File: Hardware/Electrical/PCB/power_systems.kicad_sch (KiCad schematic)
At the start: 11 parts, among them U2 LMR50410

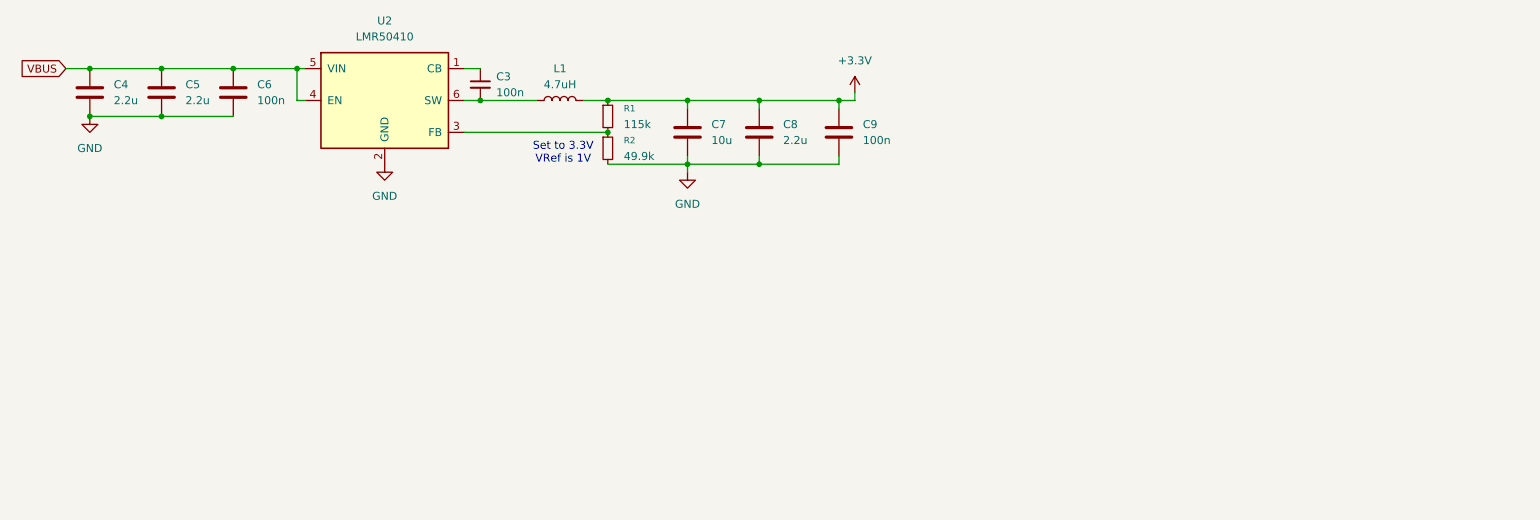
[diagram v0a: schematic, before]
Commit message: battery charger added
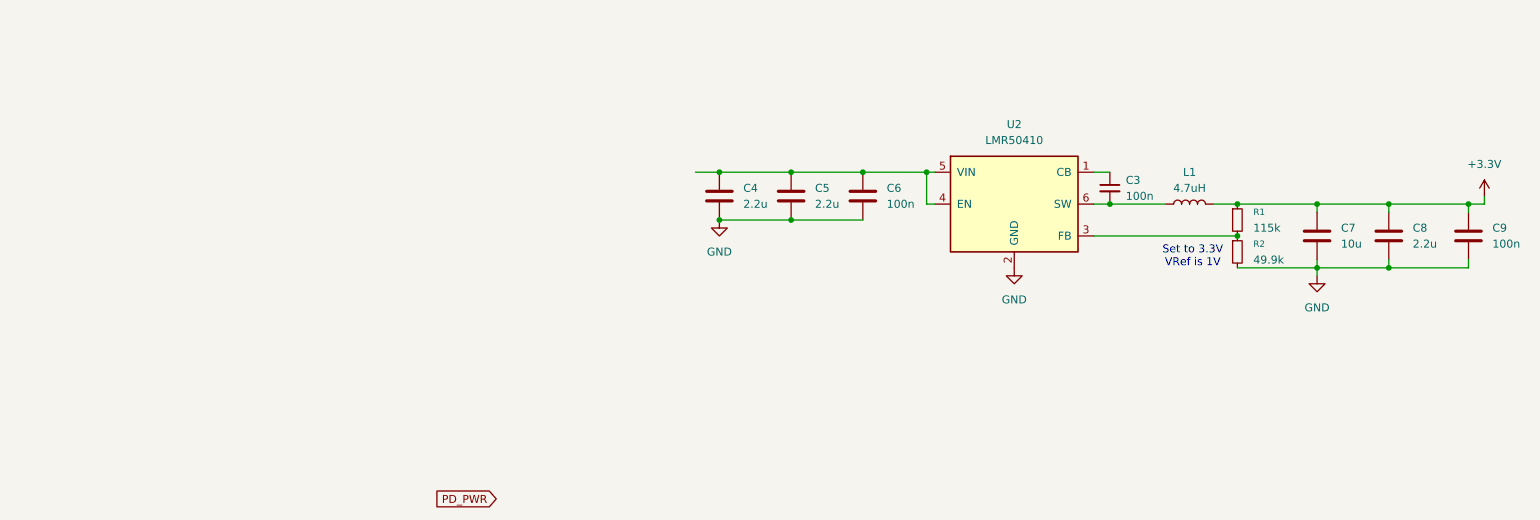
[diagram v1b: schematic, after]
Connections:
- net VBUS: no longer names the net of C4.1, C5.1, C6.1, U2.4 (EN), U2.5 (VIN)
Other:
- moved on the sheet: C3, C4, C5, C6, C7, C8, C9, L1, R1, R2, U2

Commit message: project state at start of school project
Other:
- moved on the sheet: C3, C4, C5, C6, C7, C8, C9, L1, R1, R2, U2

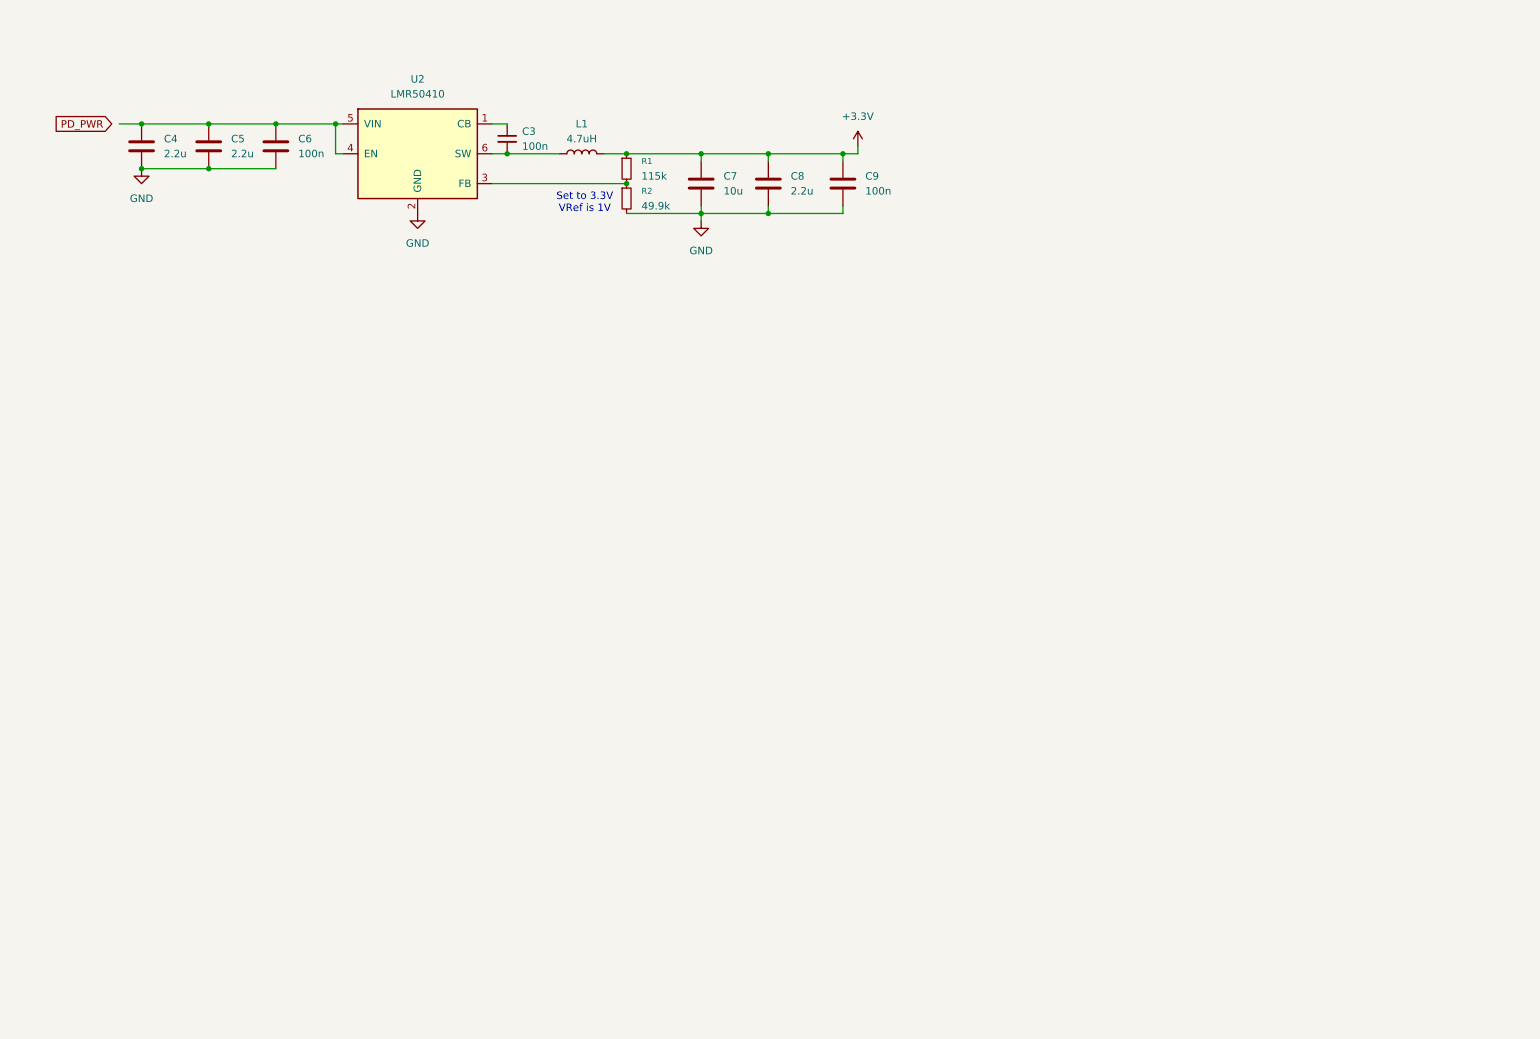
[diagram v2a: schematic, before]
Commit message: Basic Schematic finished, external connectors missing, no footprints or LCSC numbers yet
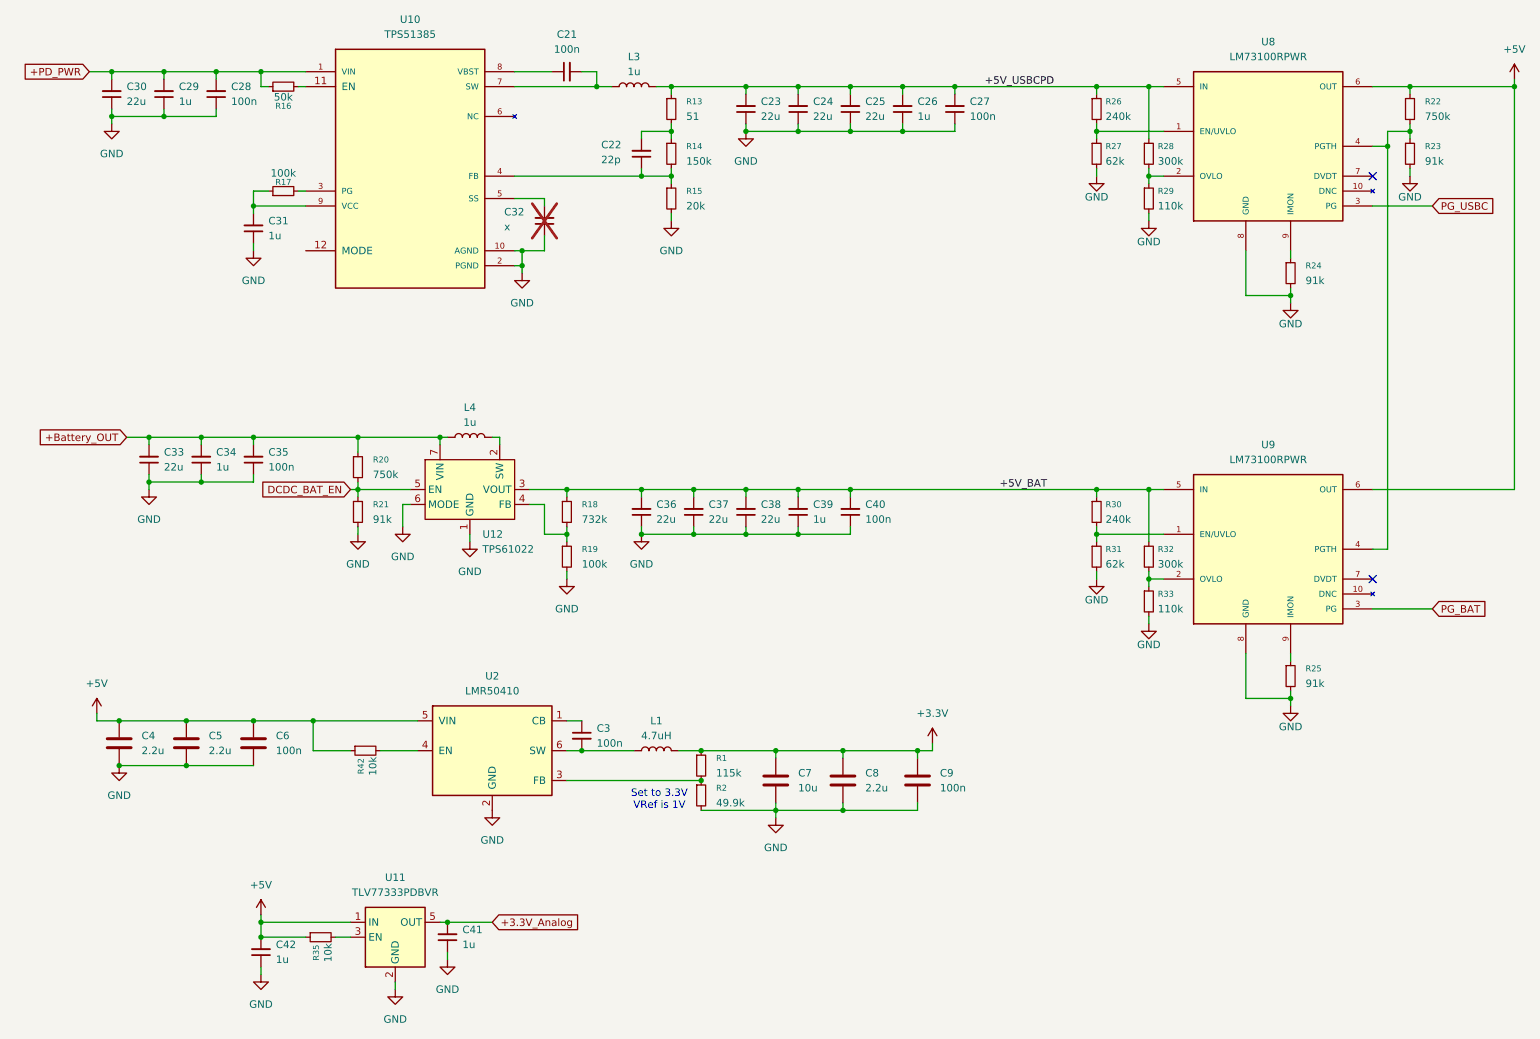
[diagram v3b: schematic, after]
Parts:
- added C21, C27, C28, C35, C40: 100n, symbol Device:C_Small
- added C22: 22p, symbol Device:C_Small
- added C23, C24, C25, C30, C33, C36, C37, C38: 22u, symbol Device:C_Small
- added C26, C29, C31, C34, C39, C41, C42: 1u, symbol Device:C_Small
- added C32: x, symbol Device:C_Small
- added L3, L4: 1u, symbol Device:L
- added R13: 51, symbol Device:R_Small
- added R14: 150k, symbol Device:R_Small
- added R15: 20k, symbol Device:R_Small
- added R16: 50k, symbol Device:R_Small
- added R17, R19: 100k, symbol Device:R_Small
- added R18: 732k, symbol Device:R_Small
- added R20, R22: 750k, symbol Device:R_Small
- added R21, R23, R24, R25: 91k, symbol Device:R_Small
- added R26, R30: 240k, symbol Device:R_Small
- added R27, R31: 62k, symbol Device:R_Small
- added R28, R32: 300k, symbol Device:R_Small
- added R29, R33: 110k, symbol Device:R_Small
- added R35, R42: 10k, symbol Device:R_Small
- added U10: TPS51385, symbol TPS51385:LM73100RPWR
- added U11: TLV77333PDBVR, Package_TO_SOT_SMD:SOT-23-5, symbol Regulator_Linear:TPS77033PDBV
- added U12: TPS61022, Package_DFN_QFN:Texas_RWU0007A_VQFN-7_2x2mm_P0.5mm, symbol Converter_DCDC:TPS61022
- added U8, U9: LM73100RPWR, LM73100RPWR:IC_LM73100RPWR, symbol LM73100RPWR:LM73100RPWR
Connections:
- net GND: now also C23.1, C24.1, C25.1, C26.1, C27.1, C28.1, C29.1, C30.1, C31.1, C32.1, C33.1, C34.1, C35.1, C36.1, C37.1, C38.1, C39.1, C40.1, C41.1, C42.1, R15.2, R19.2, R21.2, R23.2, R24.2, R25.2, R27.2, R29.2, R31.2, R33.2, U10.10 (AGND), U10.2 (PGND), U11.2 (GND), U11.4 (GND), U12.1 (GND), U12.6 (MODE), U8.8 (GND), U9.8 (GND)
- net +5V: now reaches C4.1, C5.1, C6.1, U2.5 (VIN)
- net +5V: now also C42.2, R22.1, R35.1, R42.1, U11.1 (IN), U8.6 (OUT), U9.6 (OUT); no longer U2.4 (EN)
- new net: R16.2, U10.11 (EN)
- new net: R17.2, U10.3 (PG)
- new net: C22.1, R14.2, R15.1, U10.4 (FB)
- new net: C32.2, U10.5 (SS)
- new net: C21.2, L3.1, U10.7 (SW)
- new net: C21.1, U10.8 (VBST)
- new net: C31.2, R17.1, U10.9 (VCC)
- new net: C22.2, R13.2, R14.1
- new net: R22.2, R23.1, U8.4 (PGTH), U9.4 (PGTH)
- new net: R18.2, R19.1, U12.4 (FB)
- new net: R28.2, R29.1, U8.2 (OVLO)
- new net: R30.2, R31.1, U9.1 (EN/UVLO)
- new net: R32.2, R33.1, U9.2 (OVLO)
- new net: R25.1, U9.9 (IMON)
- new net: R35.2, U11.3 (EN)
- new net: R26.2, R27.1, U8.1 (EN/UVLO)
- new net: R42.2, U2.4 (EN)
- new net: R24.1, U8.9 (IMON)
- new net: L4.2, U12.2 (SW)
- new net +3.3V_Analog: C41.2, U11.5 (OUT)
- new net +5V_BAT: C36.2, C37.2, C38.2, C39.2, C40.2, R18.1, R30.1, R32.1, U12.3 (VOUT), U9.5 (IN)
- new net +5V_USBCPD: C23.2, C24.2, C25.2, C26.2, C27.2, L3.2, R13.1, R26.1, R28.1, U8.5 (IN)
- new net +Battery_OUT: C33.2, C34.2, C35.2, L4.1, R20.1, U12.7 (VIN)
- new net +PD_PWR: C28.2, C29.2, C30.2, R16.1, U10.1 (VIN)
- new net DCDC_BAT_EN: R20.2, R21.1, U12.5 (EN)
- new net PG_BAT: U9.3 (PG)
- new net PG_USBC: U8.3 (PG)
- no-connect marks 0 -> 2
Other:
- moved on the sheet: C3, C4, C5, C6, C7, C8, C9, L1, R1, R2, U2

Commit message: layout v1 finished but not confirmed yet
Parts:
- added R49: 0, Resistor_SMD:R_0603_1608Metric, symbol Device:R_Small
- C21, C27, C28, C3, C35, C40, C6, C9: footprint (none) -> Capacitor_SMD:C_0603_1608Metric; *LCSC Part Number (none) -> C14663
- C22: footprint (none) -> Capacitor_SMD:C_0603_1608Metric; *LCSC Part Number (none) -> C1653
- C23, C24, C25, C30, C33, C36, C37, C38: footprint (none) -> Capacitor_SMD:C_1206_3216Metric; *LCSC Part Number (none) -> C12891
- C26, C29, C31, C34, C39, C41, C42: footprint (none) -> Capacitor_SMD:C_0603_1608Metric; *LCSC Part Number (none) -> C1848
- C32: footprint (none) -> Capacitor_SMD:C_0603_1608Metric
- C4, C5, C8: footprint (none) -> Capacitor_SMD:C_0603_1608Metric; *LCSC Part Number (none) -> C23630
- C7: footprint (none) -> Capacitor_SMD:C_1206_3216Metric; *LCSC Part Number (none) -> C13585
- L3, L4: value 1u -> 1uH; footprint (none) -> Inductor_SMD:L_Bourns_SRP7028A_7.3x6.6mm; *LCSC Part Number (none) -> C2847480
- R1: footprint (none) -> Resistor_SMD:R_0603_1608Metric; *LCSC Part Number (none) -> C22783
- R13: footprint (none) -> Resistor_SMD:R_0603_1608Metric; *LCSC Part Number (none) -> C23197
- R14: footprint (none) -> Resistor_SMD:R_0603_1608Metric; *LCSC Part Number (none) -> C22807
- R15: footprint (none) -> Resistor_SMD:R_0603_1608Metric; *LCSC Part Number (none) -> C4184
- R16: value 50k -> 51k; footprint (none) -> Resistor_SMD:R_0603_1608Metric; *LCSC Part Number (none) -> C23196
- R17, R19: footprint (none) -> Resistor_SMD:R_0603_1608Metric; *LCSC Part Number (none) -> C25803
- R18: footprint (none) -> Resistor_SMD:R_0603_1608Metric; *LCSC Part Number (none) -> C246003
- R2: footprint (none) -> Resistor_SMD:R_0603_1608Metric; *LCSC Part Number (none) -> C23184
- R20, R21, R22, R23, R24, R25: footprint (none) -> Resistor_SMD:R_0603_1608Metric; *LCSC Part Number (none) -> C137684
- R26, R30: footprint (none) -> Resistor_SMD:R_0603_1608Metric; *LCSC Part Number (none) -> C137765
- R27, R31: footprint (none) -> Resistor_SMD:R_0603_1608Metric; *LCSC Part Number (none) -> C137694
- R28, R32: footprint (none) -> Resistor_SMD:R_0603_1608Metric; *LCSC Part Number (none) -> C23024
- R29, R33: value 110k -> 100k; footprint (none) -> Resistor_SMD:R_0603_1608Metric; *LCSC Part Number (none) -> C25803
- R35, R42: footprint (none) -> Resistor_SMD:R_0603_1608Metric; *LCSC Part Number (none) -> C25804
- U10: footprint (none) -> TPS51385:VREG_TPS51386RJNR; *LCSC Part Number (none) -> C22418767
- U11: *LCSC Part Number (none) -> C32445874
- U12: *LCSC Part Number (none) -> TPS61022RWUR
- U2: footprint Package_SO:SOIC-8-1EP_3.9x4.9mm_P1.27mm_EP2.41x3.3mm -> Package_TO_SOT_SMD:SOT-23-6; *LCSC Part Number (none) -> C2841056
- U8, U9: footprint LM73100RPWR:IC_LM73100RPWR -> LM73100:IC_LM73100RPWR; *LCSC Part Number (none) -> C3210761
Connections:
- net at U10.12 (MODE): now also R49.1
- net at C31.2, R17.1, U10.9 (VCC): now also R49.2
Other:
- moved on the sheet: C31
